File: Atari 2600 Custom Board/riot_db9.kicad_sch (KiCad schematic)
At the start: 0 parts

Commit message: Added main ICs to schematic
Added main ICs to schematic
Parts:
- added U3: ~, symbol Atari2600_Library:6532
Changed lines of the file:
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@@
 	(generator_version "8.0")
 	(paper "A4")
+	(symbol
+		(lib_id "Atari2600_Library:6532")
+		(at 102.87 54.61 0)
+		(unit 1)
+		(exclude_from_sim no)
+		(in_bom yes)
+		(on_board yes)
+		(dnp no)
+		(fields_autoplaced yes)
+		(property "Reference" "U3"
+			(at 110.3679 50.8 0)
+			(effects
+				(font
+					(size 1.27 1.27)
+				)
+			)
+		)
+		(property "Value" "~"
+			(at 110.3679 53.34 0)
+			(effects
+				(font
+					(size 1.27 1.27)
+				)
+			)
+		)
+		(property "Footprint" ""
+			(at 100.33 54.61 0)
+			(effects
+				(font
+					(size 1.27 1.27)
+				)
+				(hide yes)
+			)
+		)
+		(property "Datasheet" ""
+			(at 100.33 54.61 0)
+			(effects
+				(font
+					(size 1.27 1.27)
+				)
+				(hide yes)
+			)
+		)
+		(property "Description" ""
+			(at 100.33 54.61 0)
+			(effects
+				(font
+					(size 1.27 1.27)
+				)
+				(hide yes)
+			)
+		)
+		(pin "28"
+		)
+		(pin "26"
+		)
+		(pin "20"
+		)
+		(pin "18"
+		)
+		(pin "27"
+		)
+		(pin "16"
+		)
+		(pin "5"
+		)
+		(pin "12"
+		)
+		(pin "40"
+		)
+		(pin "6"
+		)
+		(pin "7"
+		)
+		(pin "31"
+		)
+		(pin "9"
+		)
+		(pin "35"
+		)
+		(pin "33"
+		)
+		(pin "11"
+		)
+		(pin "39"
+		)
+		(pin "17"
+		)
+		(pin "30"
+		)
+		(pin "36"
+		)
+		(pin "4"
+		)
+		(pin "8"
+		)
+		(pin "13"
+		)
+		(pin "34"
+		)
+		(pin "10"
+		)
+		(pin "21"
+		)
+		(pin "38"
+		)
+		(pin "2"
+		)
+		(pin "19"
+		)
+		(pin "29"
+		)
+		(pin "24"
+		)
+		(pin "32"
+		)
+		(pin "1"
+		)
+		(pin "37"
+		)
+		(pin "25"
+		)
+		(pin "23"
+		)
+		(pin "3"
+		)
+		(pin "22"
+		)
+		(pin "14"
+		)
+		(pin "15"
+		)
+		(instances
+			(project "atari2600"
+				(path "/d26a1e82-f8cb-48a3-8cce-edbb66ba228a/26ae4fed-9b89-427f-9909-2070ce671822"
+					(reference "U3")
+					(unit 1)
+				)
+			)
+		)
+	)
 )

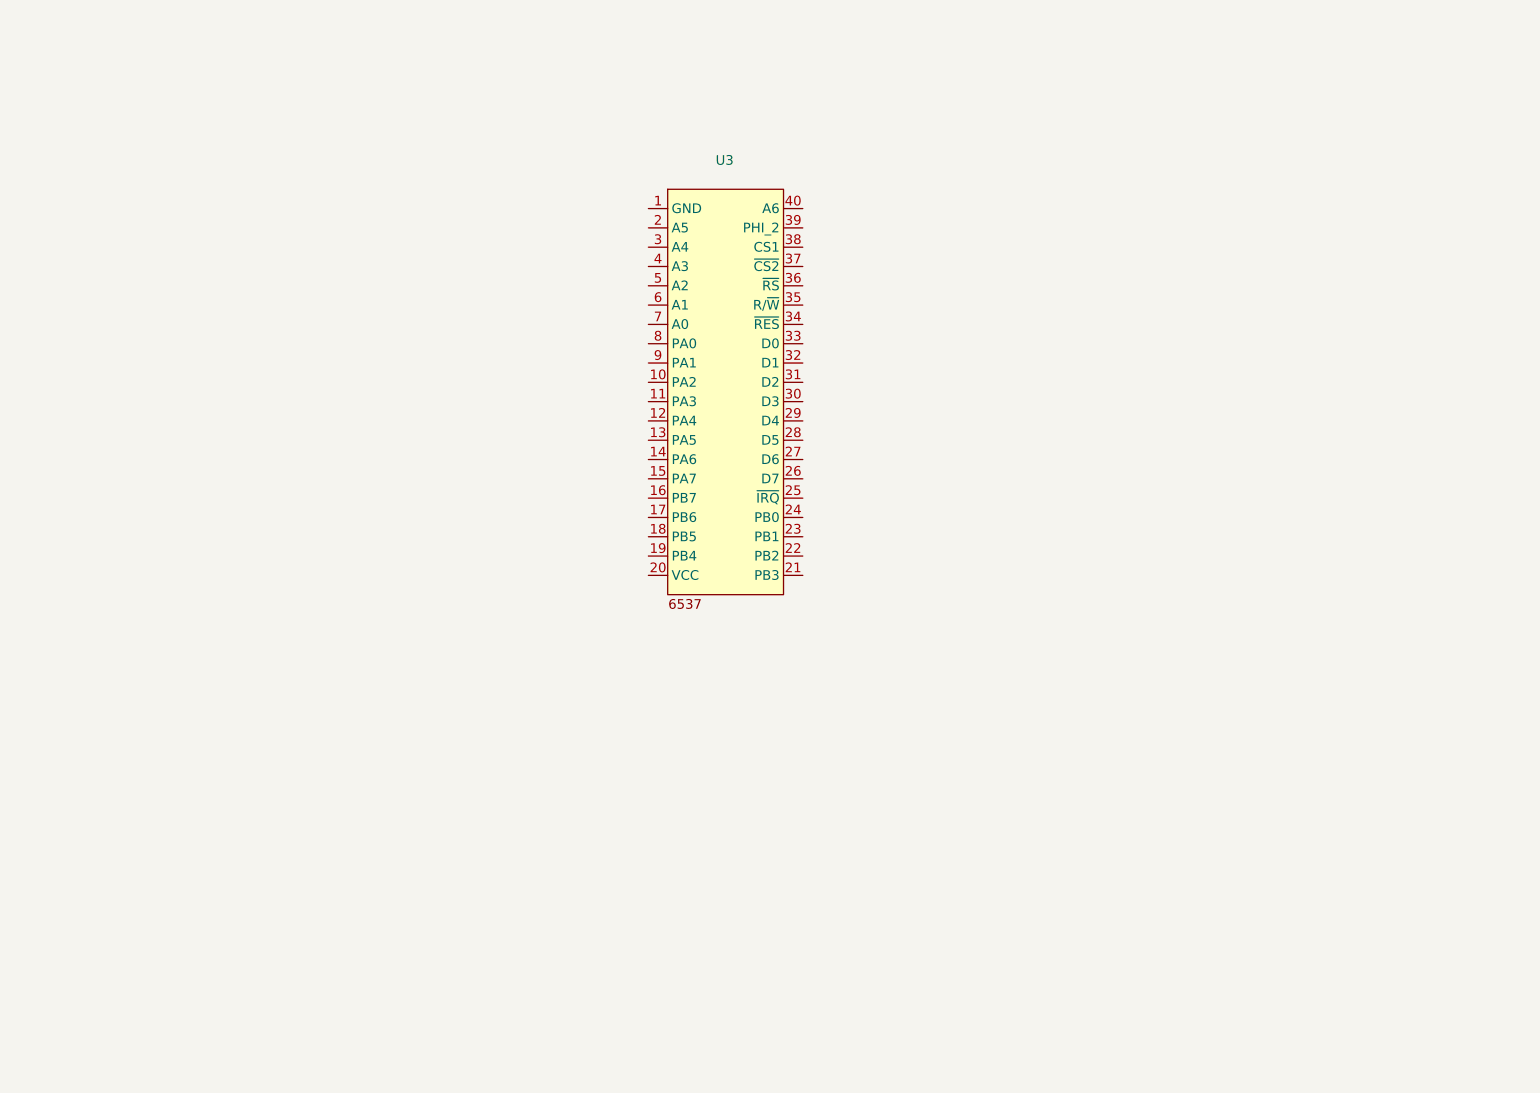
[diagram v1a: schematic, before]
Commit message: Added RIOT and DB9 schematic
Added RIOT and DB9 schematic
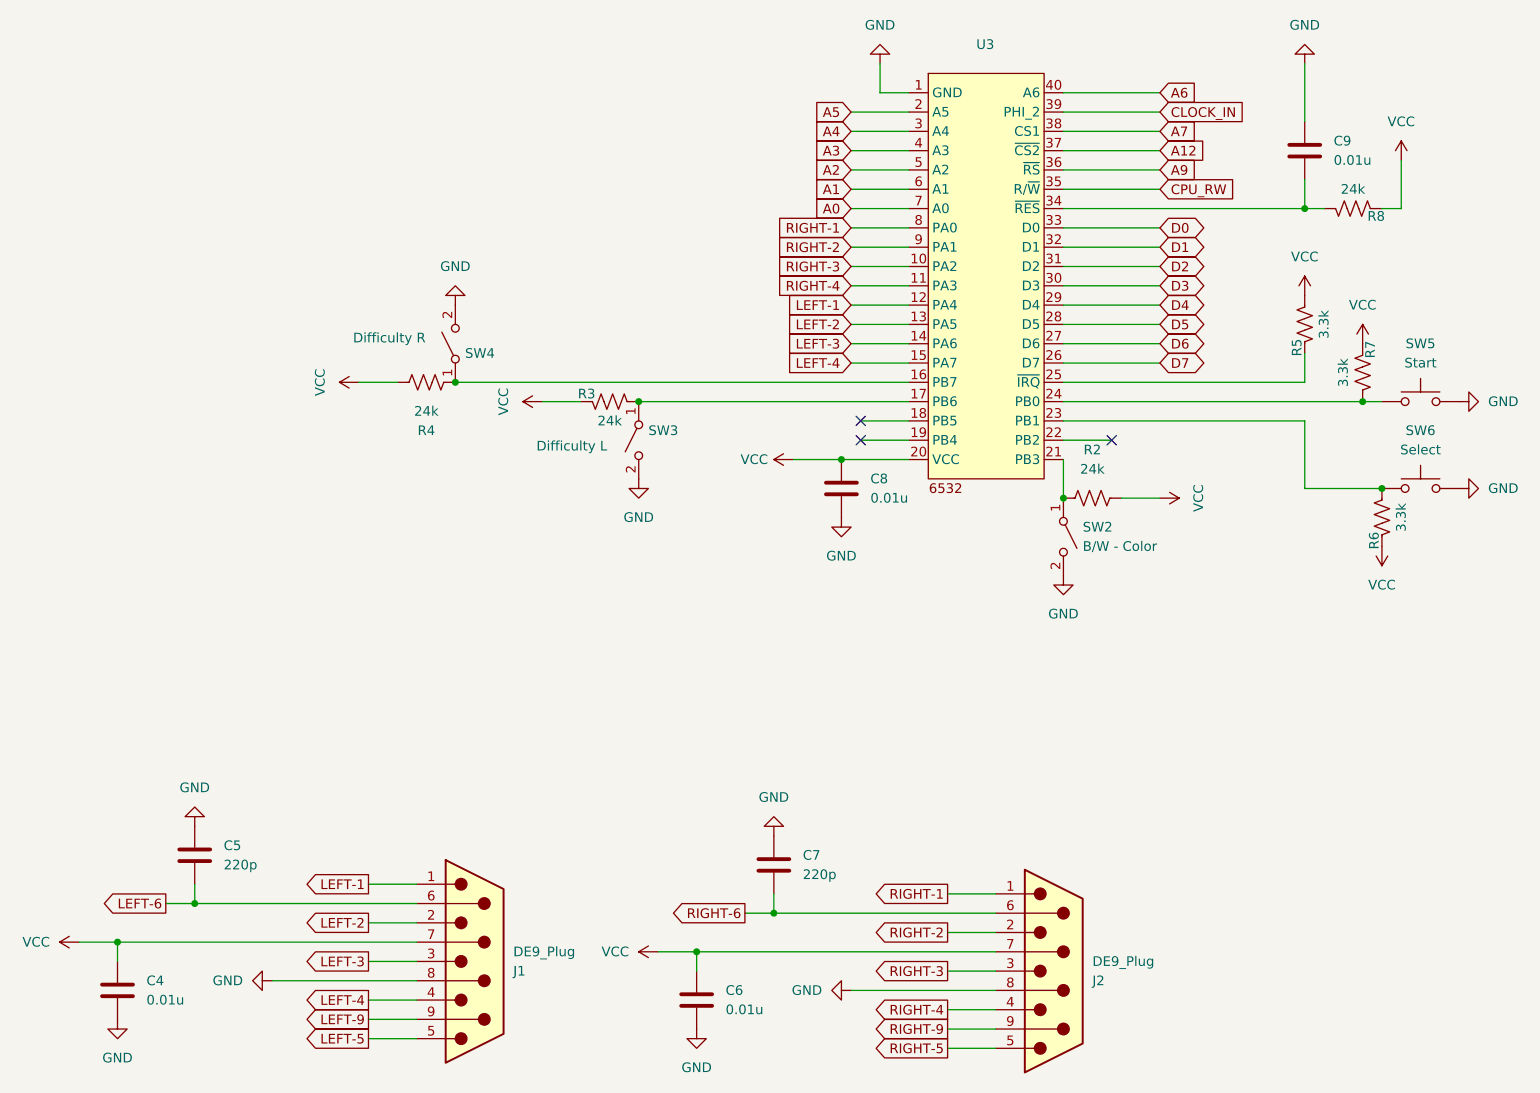
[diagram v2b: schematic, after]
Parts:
- added C4, C6, C8, C9: 0.01u, symbol Device:C
- added C5, C7: 220p, symbol Device:C
- added J1, J2: DE9_Plug, symbol Connector:DE9_Plug
- added R2, R3, R4, R8: 24k, Resistor_SMD:R_0805_2012Metric_Pad1.20x1.40mm_HandSolder, symbol Device:R_US
- added R5, R6, R7: 3.3k, Resistor_SMD:R_0805_2012Metric_Pad1.20x1.40mm_HandSolder, symbol Device:R_US
- added SW2: B/W - Color, symbol Switch:SW_SPST
- added SW3: Difficulty L, symbol Switch:SW_SPST
- added SW4: Difficulty R, symbol Switch:SW_SPST
- added SW5: Start, symbol Switch:SW_Push
- added SW6: Select, symbol Switch:SW_Push
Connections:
- net GND: now reaches U3.1 (GND)
- net GND: now also C4.2, C5.1, C6.2, C7.1, C8.2, C9.1, J1.8, J2.8, SW2.2 (B), SW3.2 (B), SW4.2 (B), SW5.2, SW6.2
- net RIGHT-3: now reaches U3.10 (PA2)
- net RIGHT-3: now also J2.3
- net RIGHT-4: now reaches U3.11 (PA3)
- net RIGHT-4: now also J2.4
- net LEFT-1: now reaches U3.12 (PA4)
- net LEFT-1: now also J1.1
- net LEFT-2: now reaches U3.13 (PA5)
- net LEFT-2: now also J1.2
- net LEFT-3: now reaches U3.14 (PA6)
- net LEFT-3: now also J1.3
- net LEFT-4: now reaches U3.15 (PA7)
- net LEFT-4: now also J1.4
- net at U3.16 (PB7): now also R4.1, SW4.1 (A)
- net at U3.17 (PB6): now also R3.1, SW3.1 (A)
- net A5: now reaches U3.2 (A5)
- net VCC: now reaches U3.20 (VCC)
- net VCC: now also C4.1, C6.1, C8.1, J1.7, J2.7, R2.2, R3.2, R4.2, R5.1, R6.2, R7.2, R8.2
- net at U3.21 (PB3): now also R2.1, SW2.1 (A)
- net at U3.23 (PB1): now also R6.1, SW6.1
- net at U3.24 (PB0): now also R7.1, SW5.1
- net at U3.25 (~{IRQ}): now also R5.2
- net D7: now reaches U3.26 (D7)
- net D6: now reaches U3.27 (D6)
- net D5: now reaches U3.28 (D5)
- net D4: now reaches U3.29 (D4)
- net A4: now reaches U3.3 (A4)
- net D3: now reaches U3.30 (D3)
- net D2: now reaches U3.31 (D2)
- net D1: now reaches U3.32 (D1)
- net D0: now reaches U3.33 (D0)
- net at U3.34 (~{RES}): now also C9.2, R8.1
- net CPU_RW: now reaches U3.35 (R/~{W})
- net A9: now reaches U3.36 (~{RS})
- net A12: now reaches U3.37 (~{CS2})
- net A7: now reaches U3.38 (CS1)
- net CLOCK_IN: now reaches U3.39 (PHI_2)
- net A3: now reaches U3.4 (A3)
- net A6: now reaches U3.40 (A6)
- net A2: now reaches U3.5 (A2)
- net A1: now reaches U3.6 (A1)
- net A0: now reaches U3.7 (A0)
- net RIGHT-1: now reaches U3.8 (PA0)
- net RIGHT-1: now also J2.1
- net RIGHT-2: now reaches U3.9 (PA1)
- net RIGHT-2: now also J2.2
- new net LEFT-5: J1.5
- new net LEFT-6: C5.2, J1.6
- new net LEFT-9: J1.9
- new net RIGHT-5: J2.5
- new net RIGHT-6: C7.2, J2.6
- new net RIGHT-9: J2.9
- no-connect marks 0 -> 3
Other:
- moved on the sheet: U3

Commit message: Cleaned up electrical rules violations
Cleaned up electrical rules violations
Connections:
- net CLOCK_IN renamed PHI_2
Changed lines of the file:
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@@
 		)
 	)
-	(global_label "CLOCK_IN"
+	(global_label "PHI_2"
 		(shape input)
 		(at 167.64 44.45 0)
@@
 		)
 		(property "Intersheetrefs" "${INTERSHEET_REFS}"
-			(at 179.6967 44.45 0)
+			(at 176.0076 44.45 0)
 			(effects
 				(font

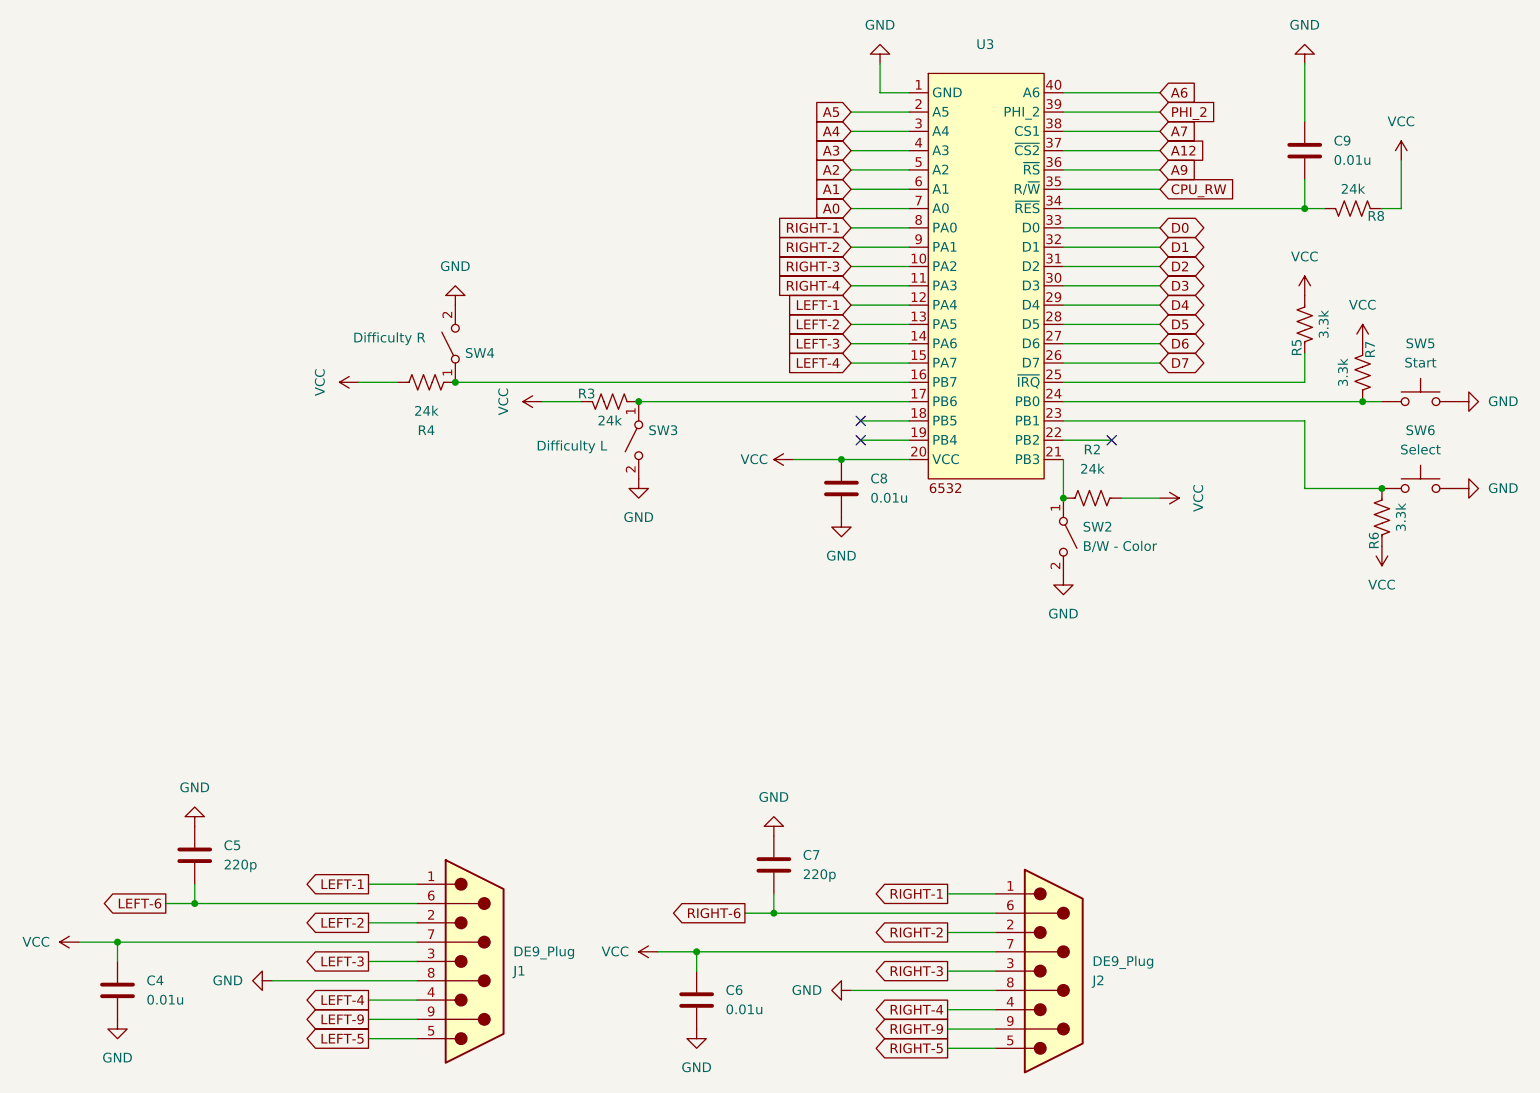
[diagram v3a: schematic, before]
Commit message: Fixed some incorrect values and re-annotated
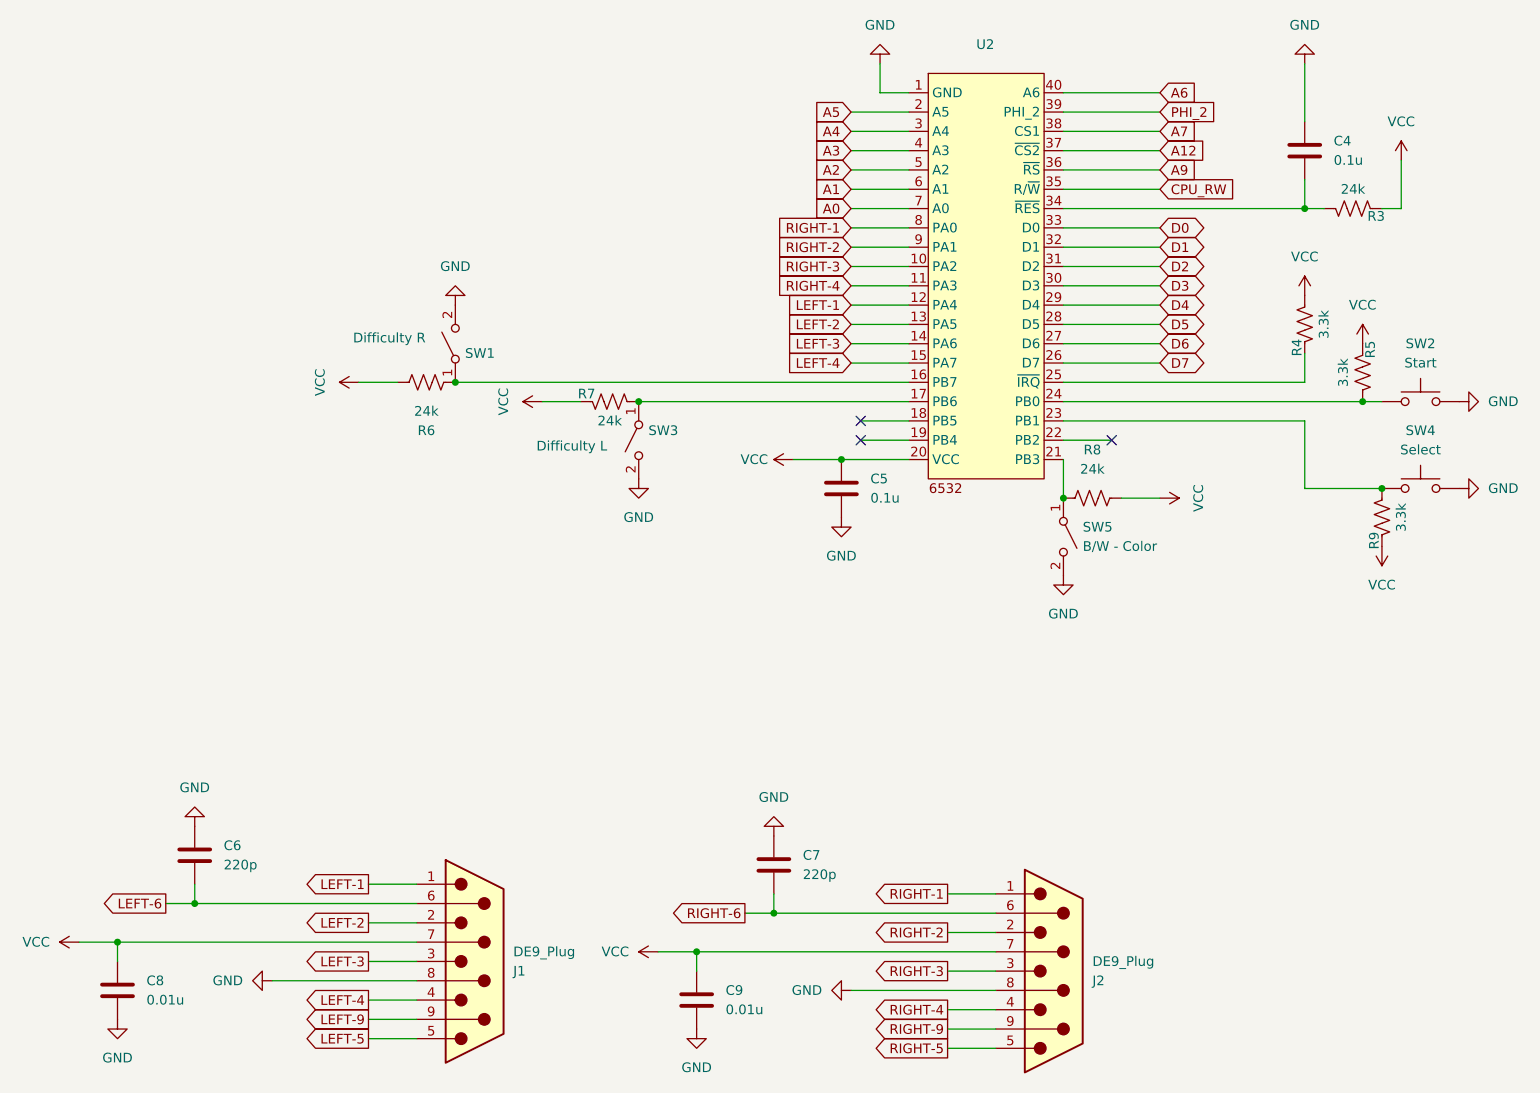
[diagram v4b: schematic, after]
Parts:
- C4: renamed from C9; value 0.01u -> 0.1u
- C5: renamed from C8; value 0.01u -> 0.1u
- renumbered C5 to C6, C4 to C8, C6 to C9, R8 to R3, R5 to R4, R7 to R5, R4 to R6, R3 to R7, R2 to R8, R6 to R9, SW4 to SW1, SW5 to SW2, SW6 to SW4, SW2 to SW5, U3 to U2

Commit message: assign footprints
assigned most footprints to schematic
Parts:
- C4, C5, C6, C7, C8, C9: footprint (none) -> Capacitor_SMD:C_0805_2012Metric_Pad1.18x1.45mm_HandSolder
- SW2, SW4: footprint (none) -> Atari2600_Libary:2600-Momentary-Switch
- SW5: footprint (none) -> Atari2600_Libary:2600-Toggle-Switch
- U2: footprint (none) -> Package_DIP:DIP-40_W15.24mm_LongPads
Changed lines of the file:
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@@
 			)
 		)
-		(property "Footprint" ""
+		(property "Footprint" "Capacitor_SMD:C_0805_2012Metric_Pad1.18x1.45mm_HandSolder"
 			(at 107.6452 165.1 0)
 			(effects
@@
 			)
 		)
-		(property "Footprint" ""
+		(property "Footprint" "Atari2600_Libary:2600-Toggle-Switch"
 			(at 154.94 100.33 0)
 			(effects
@@
 			)
 		)
-		(property "Footprint" ""
+		(property "Footprint" "Capacitor_SMD:C_0805_2012Metric_Pad1.18x1.45mm_HandSolder"
 			(at 126.6952 97.79 0)
 			(effects
@@
 			)
 		)
-		(property "Footprint" ""
+		(property "Footprint" "Atari2600_Libary:2600-Momentary-Switch"
 			(at 201.93 88.9 0)
 			(effects
@@
 			)
 		)
-		(property "Footprint" ""
+		(property "Footprint" "Capacitor_SMD:C_0805_2012Metric_Pad1.18x1.45mm_HandSolder"
 			(at 41.6052 146.05 0)
 			(effects
@@
 			)
 		)
-		(property "Footprint" ""
+		(property "Footprint" "Atari2600_Libary:2600-Momentary-Switch"
 			(at 201.93 77.47 0)
 			(effects
@@
 			)
 		)
-		(property "Footprint" ""
+		(property "Footprint" "Capacitor_SMD:C_0805_2012Metric_Pad1.18x1.45mm_HandSolder"
 			(at 31.4452 163.83 0)
 			(effects
@@
 			)
 		)
-		(property "Footprint" ""
+		(property "Footprint" "Capacitor_SMD:C_0805_2012Metric_Pad1.18x1.45mm_HandSolder"
 			(at 117.8052 147.32 0)
 			(effects
@@
 			)
 		)
-		(property "Footprint" ""
+		(property "Footprint" "Capacitor_SMD:C_0805_2012Metric_Pad1.18x1.45mm_HandSolder"
 			(at 187.6552 53.34 0)
 			(effects
@@
 			)
 		)
-		(property "Footprint" ""
+		(property "Footprint" "Package_DIP:DIP-40_W15.24mm_LongPads"
 			(at 134.62 39.37 0)
 			(effects
